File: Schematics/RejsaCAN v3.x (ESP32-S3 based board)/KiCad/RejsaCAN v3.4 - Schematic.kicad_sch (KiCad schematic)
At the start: 82 parts, among them J1 Micro-Fit 3.0 4P R/A, J2 U.FL, J3 JST-XH 4P LTE, Q1 SS8050, U1 ESP32-S3-WROOM-1(N16R8), U2 SN65HVD230DR, U3 ME2807A33M3G, U4 LMR14010ADDCR, U5 MT9700, U6 GAQY212GS, U7 LG290P03AAMD, U8 AP2112K-3.3

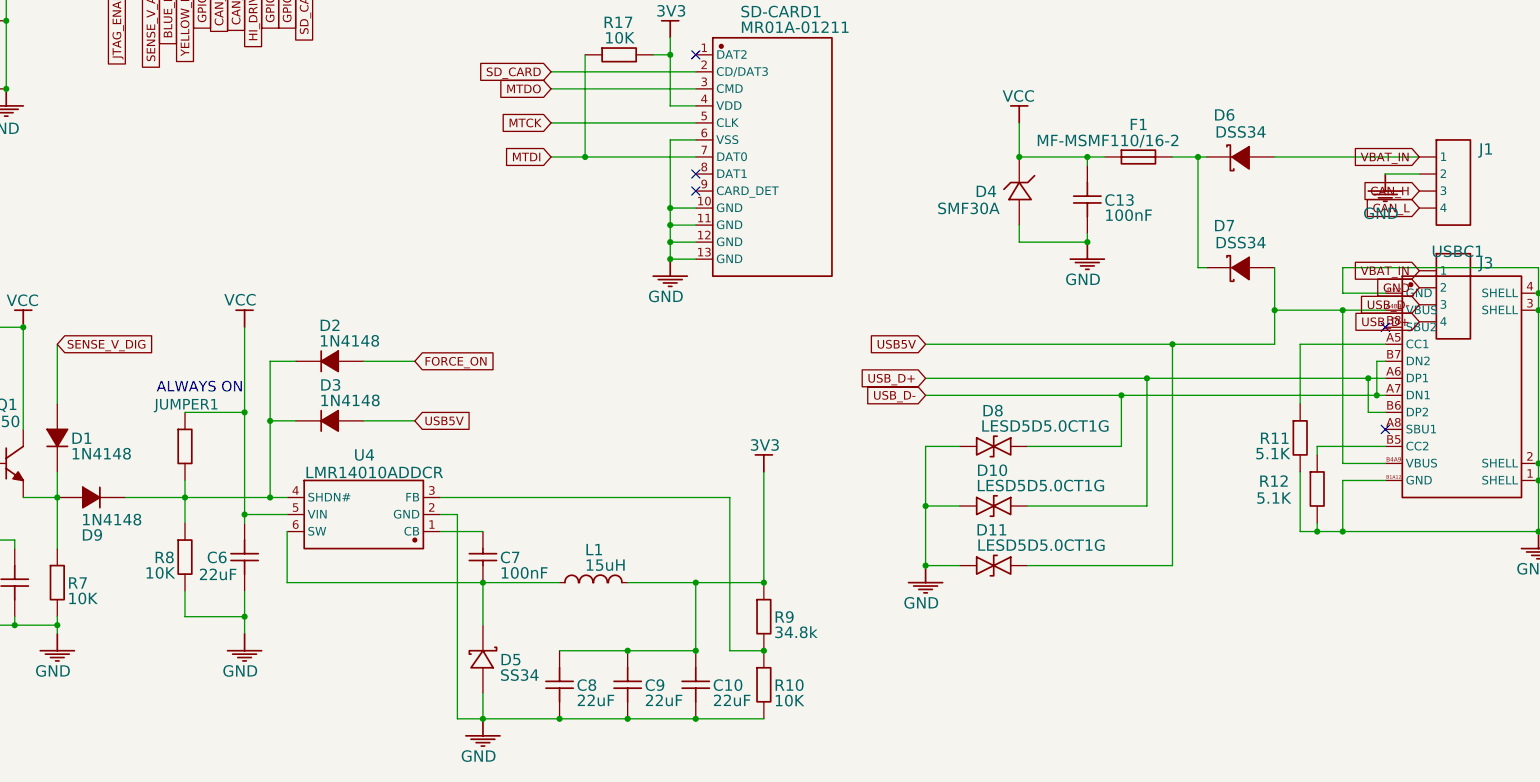
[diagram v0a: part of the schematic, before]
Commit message: Front end rated for real automotive transients: 5-24V, 33V ceiling
The board claimed 5-24V but none of its three protection devices supported it.
Owner confirmed the operating reality -- a 12V system running at 14V with
spikes -- and confirmed the installation constraint the fix depends on.

The chain that sets the rating: a 12V-system SUPPRESSED load dump is 35V for
40-400ms, so the clamp must not conduct at 35V -> 33V standoff -> VC 53.3V at
25C, ~56V hot -> the regulator must survive ~56V. That single requirement
forces every part below.

  U4   LMR14010A -> LMR51610X    45V abs max could not take any clamp that
                                 survives a 35V dump. Same SOT-23-6 land.
  R9   34.8k -> 69.8k            The new part's reference is 0.800V, not
  R10  10k   -> 22.1k            0.765V. Leaving the divider alone yields
                                 3.58V against the ESP32-S3's 3.6V absolute
                                 maximum. This would have cooked the module.
  D4   SMF30A -> SMBJ33CA        200W 10/1000us cannot address a millisecond
       and moved VCC -> VBAT_IN  event, and its clamp sat ABOVE the buck's
                                 abs max. Bidirectional, and now upstream of
                                 the fuse and blocking diode so it also covers
                                 reverse transients.
  D6   DSS34 -> SS310            40V cannot block a -53V clamp.
  D7   DSS34 -> SS310            Same node, same exposure.
  F1   MF-MSMF110/16-2 -> 2A/72V 16V max on a rail that sees a 24V jump start.
       PPTC -> time-delay fuse   It also derates to 0.60A at 85C against ~0.6A
                                 demand, so it nuisance-trips in an engine bay
                                 today. No PPTC family reaches 33V at 0.6A hot.
  F3   NEW 4A/72V                J3 fed an external LTE module from raw battery
                                 with no protection at all; the trace was the
                                 only curren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
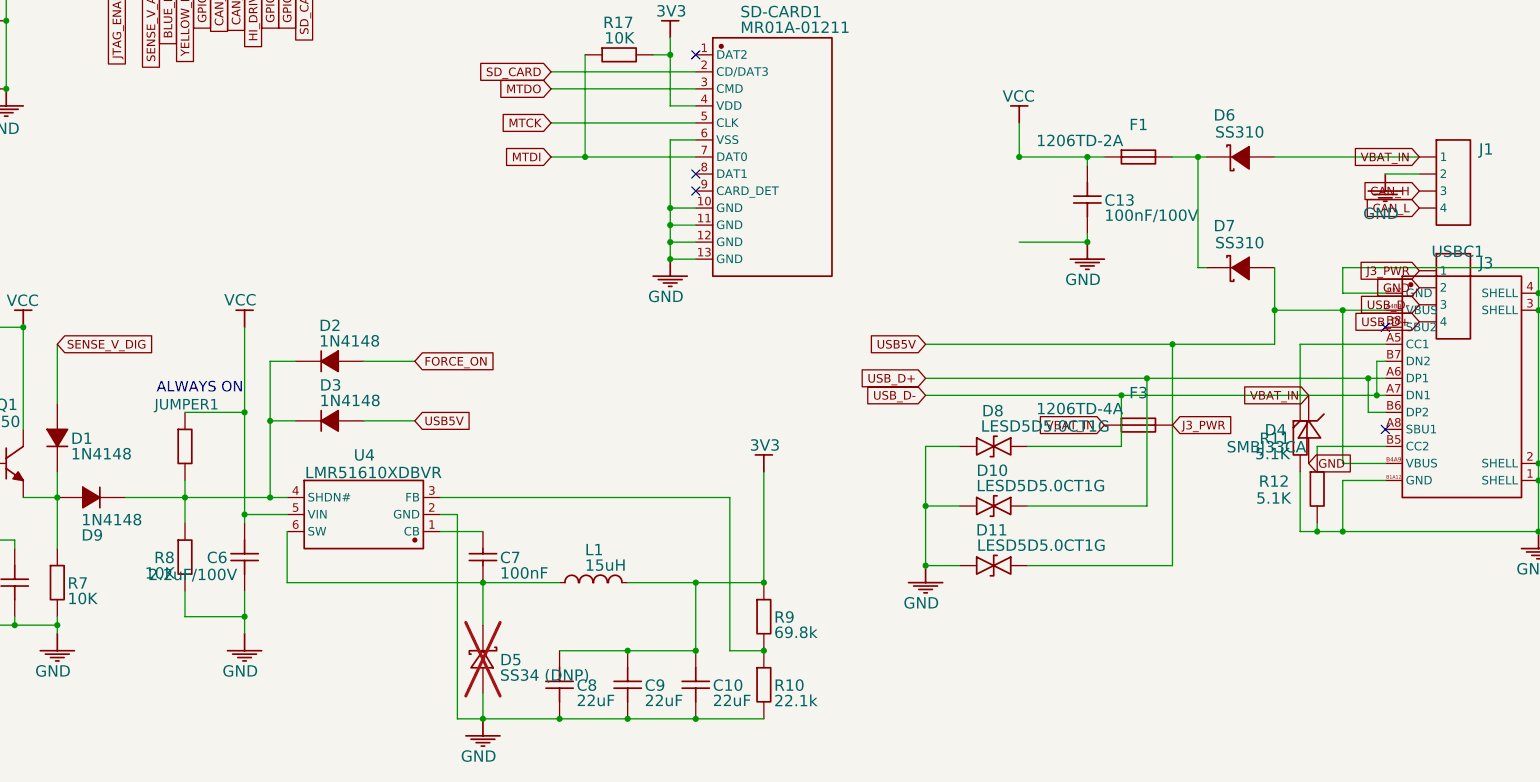
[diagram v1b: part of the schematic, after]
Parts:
- added F3: 1206TD-4A, Fuse:Fuse_1206_3216Metric, symbol MF-MSMF110/16-2
- C13: value 100nF -> 100nF/100V; footprint Capacitor_SMD:C_0402_1005Metric -> Capacitor_SMD:C_0603_1608Metric; Supplier Part C307331 -> (none)
- C6: value 22uF -> 2.2uF/100V; footprint Capacitor_SMD:C_0805_2012Metric -> Capacitor_SMD:C_1210_3225Metric; Supplier Part C602037 -> (none)
- D4: value SMF30A -> SMBJ33CA; footprint Diode_SMD:D_SOD-123 -> Diode_SMD:D_SMB; Supplier Part C366558 -> (none)
- D5: value SS34 -> SS34 (DNP); now not fitted
- D6, D7: value DSS34 -> SS310; footprint Diode_SMD:D_SOD-123 -> Diode_SMD:D_SMA; Supplier Part C84632 -> (none)
- F1: value MF-MSMF110/16-2 -> 1206TD-2A; footprint RejsaCAN:Fuse_1812_RejsaCAN_3.706mm -> Fuse:Fuse_1206_3216Metric; Supplier Part C210834 -> (none)
- R10: value 10K -> 22.1k; Supplier Part C25744 -> (none)
- R9: value 34.8k -> 69.8k; Supplier Part C25779 -> (none)
- U4: value LMR14010ADDCR -> LMR51610XDBVR
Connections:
- net USB_D-: now also D4.1, D6.2 (A), J1.1, F3.1
- net VCC: no longer D4.1
- net USB5V renamed J3_PWR
- net J3_PWR: now also J3.1, F3.2
- removed net VBAT_IN: D6.2 (A), J1.1, J3.1
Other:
- moved on the sheet: D4
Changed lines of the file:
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@@
 	(wire
 		(pts
-			(xy 200.66 121.92) (xy 200.66 119.38)
-		)
-		(stroke
-			(width 0)
-			(type default)
-		)
-	)
-	(wire
-		(pts
 			(xy 190.5 40.64) (xy 194.31 40.64)
 		)
@@
 			)
 		)
-		(property "Value" "10K"
+		(property "Value" "22.1k"
 			(at 164.084 189.3951 0)
 			(show_name no)
@@
 			)
 		)
-		(property "Supplier Part" "C25744"
+		(property "Supplier Part" ""
 			(at 162.56 187.96 0)
 			(hide yes)
@@
 			)
 		)
-		(property "Value" "22uF"
+		(property "Value" "2.2uF/100V"
 			(at 83.9978 170.5737 0)
 			(show_name no)
@@
 			)
 		)
-		(property "Footprint" "Capacitor_SMD:C_0805_2012Metric"
+		(property "Footprint" "Capacitor_SMD:C_1210_3225Metric"
 			(at 85.09 168.91 0)
 			(hide yes)
@@
 			)
 		)
-		(property "Supplier Part" "C602037"
+		(property "Supplier Part" ""
 			(at 85.09 168.91 0)
 			(hide yes)
@@
 			)
 		)
-		(property "Value" "LMR14010ADDCR"
+		(property "Value" "LMR51610XDBVR"
 			(at 94.107 155.3591 0)
 			(show_name no)
@@
 			)
 		)
-		(property "Value" "MF-MSMF110/16-2"
+		(property "Value" "1206TD-2A"
 			(at 203.2 105.8291 0)
 			(show_name no)
@@
 			)
 		)
-		(property "Footprint" "RejsaCAN:Fuse_1812_RejsaCAN_3.706mm"
+		(property "Footprint" "Fuse:Fuse_1206_3216Metric"
 			(at 218.44 109.22 0)
 			(hide yes)
@@
 			)
 		)
-		(property "Supplier Part" "C210834"
+		(property "Supplier Part" ""
 			(at 218.44 109.22 0)
 			(hide yes)
@@
 			)
 		)
-		(property "Value" "34.8k"
+		(property "Value" "69.8k"
 			(at 164.084 179.2097 0)
 			(show_name no)
@@
 			)
 		)
-		(property "Supplier Part" "C25779"
+		(property "Supplier Part" ""
 			(at 162.56 177.8 0)
 			(hide yes)
@@
 			)
 		)
-		(property "Value" "100nF"
+		(property "Value" "100nF/100V"
 			(at 213.36 116.9797 0)
 			(show_name no)
@@
 			)
 		)
-		(property "Footprint" "Capacitor_SMD:C_0402_1005Metric"
+		(property "Footprint" "Capacitor_SMD:C_0603_1608Metric"
 			(at 210.82 115.57 0)
 			(hide yes)
@@
 			)
 		)
-		(property "Supplier Part" "C307331"
+		(property "Supplier Part" ""
 			(at 210.82 115.57 0)
 			(hide yes)
@@
 			)
 		)
-		(property "Value" "DSS34"
+		(property "Value" "SS310"
 			(at 229.87 121.0691 0)
 			(show_name no)
@@
 			)
 		)
-		(property "Footprint" "Diode_SMD:D_SOD-123"
+		(property "Footprint" "Diode_SMD:D_SMA"
 			(at 233.68 125.73 0)
 			(hide yes)
@@
 			)
 		)
-		(property "Supplier Part" "C84632"
+		(property "Supplier Part" ""
 			(at 233.68 125.73 0)
 			(hide yes)
@@
 	(symbol
 		(lib_id "SMF30A_C366558")
-		(at 200.66 114.3 0)
+		(at 243.84 149.86 0)
 		(unit 0)
 		(body_style 0)
@@
 		(dnp no)
 		(property "Reference" "D4"
-			(at 194.0814 113.4237 0)
+			(at 237.261 148.984 0)
 			(show_name no)
 			(do_not_autoplace no)
@@
 			)
 		)
-		(property "Value" "SMF30A"
-			(at 188.4172 115.9637 0)
+		(property "Value" "SMBJ33CA"
+			(at 231.597 151.524 0)
 			(show_name no)
 			(do_not_autoplace no)
@@
 			)
 		)
-		(property "Footprint" "Diode_SMD:D_SOD-123"
-			(at 200.66 114.3 0)
+		(property "Footprint" "Diode_SMD:D_SMB"
+			(at 243.84 149.86 0)
 			(hide yes)
 			(show_name no)
@@
 		)
 		(property "Datasheet" ""
-			(at 200.66 114.3 0)
+			(at 243.84 149.86 0)
 			(hide yes)
 			(show_name no)
@@
 		)
 		(property "Description" ""
-			(at 200.66 114.3 0)
+			(at 243.84 149.86 0)
 			(hide yes)
 			(show_name no)
@@
 		)
 		(property "Manufacturer Part" "SMF30A"
-			(at 200.66 114.3 0)
+			(at 243.84 149.86 0)
 			(hide yes)
 			(show_name no)
@@
 		)
 		(property "Manufacturer" "DOWO"
-			(at 200.66 114.3 0)
+			(at 243.84 149.86 0)
 			(hide yes)
 			(show_name no)
@@
 			)
 		)
-		(property "Supplier Part" "C366558"
-			(at 200.66 114.3 0)
+		(property "Supplier Part" ""
+			(at 243.84 149.86 0)
 			(hide yes)
 			(show_name no)
@@
 		)
 		(property "Supplier" "LCSC"
-			(at 200.66 114.3 0)
+			(at 243.84 149.86 0)
 			(hide yes)
 			(show_name no)
@@
 		(on_board yes)
 		(in_pos_files yes)
-		(dnp no)
+		(dnp yes)
 		(property "Reference" "D5"
 			(at 123.19 183.2737 0)
@@
 			)
 		)
-		(property "Value" "SS34"
+		(property "Value" "SS34 (DNP)"
 			(at 123.19 185.5851 0)
 			(show_name no)
@@
 			)
 		)
-		(property "Value" "DSS34"
+		(property "Value" "SS310"
 			(at 229.87 104.5591 0)
 			(show_name no)
@@
 			)
 		)
-		(property "Footprint" "Diode_SMD:D_SOD-123"
+		(property "Footprint" "Diode_SMD:D_SMA"
 			(at 233.68 109.22 0)
 			(hide yes)
@@
 			)
 		)
-		(property "Supplier Part" "C84632"
+		(property "Supplier Part" ""
 			(at 233.68 109.22 0)
 			(hide yes)
@@
 		)
 	)
-	(global_label "VBAT_IN"
+	(global_label "J3_PWR"
 		(shape input)
 		(at 260.35 126.19 180)
@@
 		)
 	)
+	(global_label "VBAT_IN"
+		(shape input)
+		(at 243.84 144.78 180)
+		(effects
+			(font
+				(size 1.27 1.27)
+			)
+			(justify right)
+		)
+	)
+	(global_label "GND"
+		(shape input)
+		(at 243.84 154.94 0)
+		(effects
+			(font
+				(size 1.27 1.27)
+			)
+			(justify left)
+		)
+	)
+	(symbol
+		(lib_id "MF-MSMF110/16-2")
+		(at 218.44 149.22 0)
+		(unit 0)
+		(body_style 0)
+		(exclude_from_sim no)
+		(in_bom yes)
+		(on_board yes)
+		(in_pos_files yes)
+		(dnp no)
+		(property "Reference" "F3"
+			(at 217.068 143.441 0)
+			(show_name no)
+			(do_not_autoplace no)
+			(effects
+				(font
+					(face "Arial")
+					(size 1.6891 1.6891)
+				)
+				(justify left top)
+			)
+		)
+		(property "Value" "1206TD-4A"
+			(at 203.2 145.829 0)
+			(show_name no)
+			(do_not_autoplace no)
+			(effects
+				(font
+					(face "Arial")
+					(size 1.6891 1.6891)
+				)
+				(justify left top)
+			)
+		)
+		(property "Footprint" "Fuse:Fuse_1206_3216Metric"
+			(at 218.44 149.22 0)
+			(hide yes)
+			(show_name no)
+			(do_not_autoplace no)
+			(effects
+				(font
+					(size 1.27 1.27)
+				)
+			)
+		)
+		(property "Datasheet" ""
+			(at 218.44 149.22 0)
+			(hide yes)
+			(show_name no)
+			(do_not_autoplace no)
+			(effects
+				(font
+					(size 1.27 1.27)
+				)
+			)
+		)
+		(property "Description" ""
+			(at 218.44 149.22 0)
+			(hide yes)
+			(show_name no)
+			(do_not_autoplace no)
+			(effects
+				(font
+					(size 1.27 1.27)
+				)
+			)
+		)
+		(property "Manufacturer Part" "MF-MSMF110/16-2"
+			(at 218.44 149.22 0)
+			(hide yes)
+			(show_name no)
+			(do_not_autoplace no)
+			(effects
+				(font
+					(size 1.27 1.27)
+				)
+			)
+		)
+		(property "Manufacturer" "BOURNS"
+			(at 218.44 149.22 0)
+			(hide yes)
+			(show_name no)
+			(do_not_autoplace no)
+			(effects
+				(font
+					(size 1.27 1.27)
+				)
+			)
+		)
+		(property "Supplier Part" ""
+			(at 218.44 149.22 0)
+			(hide yes)
+			(show_name no)
+			(do_not_autoplace no)
+			(effects
+				(font
+					(size 1.27 1.27)
+				)
+			)
+		)
+		(property "Supplier" "LCSC"
+			(at 218.44 149.22 0)
+			(hide yes)
+			(show_name no)
+			(do_not_autoplace no)
+			(effects
+				(font
+					(size 1.27 1.27)
+				)
+			)
+		)
+		(pin "1"
+		)
+		(pin "2"
+		)
+		(instances
+			(project "RejsaCAN v3.4 - Schematic"
+				(path "/16c2f03a-5652-4050-b62b-75ebc6e5d249"
+					(reference "F3")
+					(unit 0)
+				)
+			)
+		)
+	)
+	(global_label "VBAT_IN"
+		(shape input)
+		(at 213.36 149.22 180)
+		(effects
+			(font
+				(size 1.27 1.27)
+			)
+			(justify right)
+		)
+	)
+	(global_label "J3_PWR"
+		(shape input)
+		(at 223.52 149.22 0)
+		(effects
+			(font
+				(size 1.27 1.27)
+			)
+			(justify left)
+		)
+	)

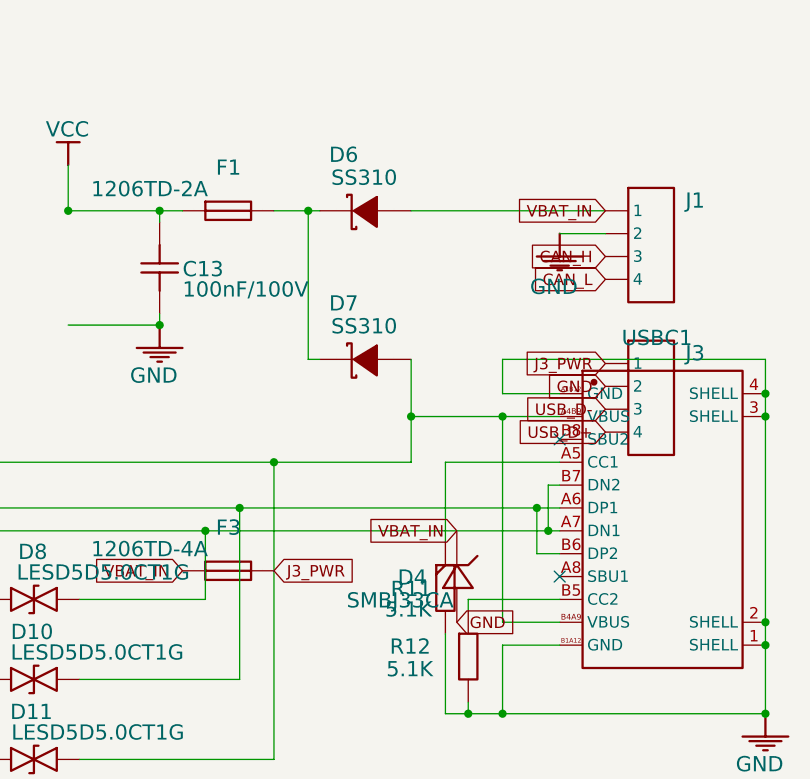
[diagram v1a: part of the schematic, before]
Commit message: PCB: rebuild for the new front end, spread the power corner, re-route
DRC clean of every electrical and fabrication class. 4 connections open, all
in the power section; finish them in the GUI's interactive router, which can
shove existing traces where the Python API cannot.

  947 tracks, 80 vias, 87 footprints
  PWR_plane  875.2 mm
  F.Cu       872.7 mm
  B.Cu       267.3 mm
  GND_plane  0 mm  -- held solid as the RF reference

Smaller packages, chosen on the numbers rather than to save space:

  D4  SMB -> SMA   SMAJ33CA. The actual pulse-1 energy is 61 mJ; SMAJ's 400 W
                   is 0.4 J, a 6.5x margin. The SMB had been sized off a figure
                   the synthesis itself flagged as ~10x high (it used 24 V
                   system pulse levels on a 12 V board).
  D6  SMA -> SOD-123FL  SS110, 100 V / 1 A. D6 carries only this board's own
  D7  SMA -> SOD-123FL  draw; the LTE branch taps VBAT_IN upstream of D6 and
                   has its own fuse, so 3 A was sizing for current that never
                   flows through it.

That took the component-area delta from +47 mm2 to +9.1 mm2 and removed the
need to grow the board.

Power corner spread. 12 low-speed parts (U3, R4, R5, R19, R6, C5, D1, D2, D9,
Q1, R7, R8 -- the battery-sense divider and the auto-shutdown chain) moved out
of the congested area. U4, L1 and D5 stayed put deliberately: they are the
switching loop, and moving them would lengthen the SW node, which already sits
45 mm from a GNSS receiver.

The split is by circuit type, not geography. The sense and shutdown circuits
are high-impedance and indifferent to a few extra millimetres; the buck is not.

Effect: the router finished in 131 s against 310-660 s on every previous
attempt, and courtyard overlaps fell 43 -> 26.

Placement was searched, not hand-picked. Three earlier attempts at choosing
coordinates by eye put C13 on the feedback divider, stacked the RF parts into
each other, and read one row of a free-space map as if the block 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
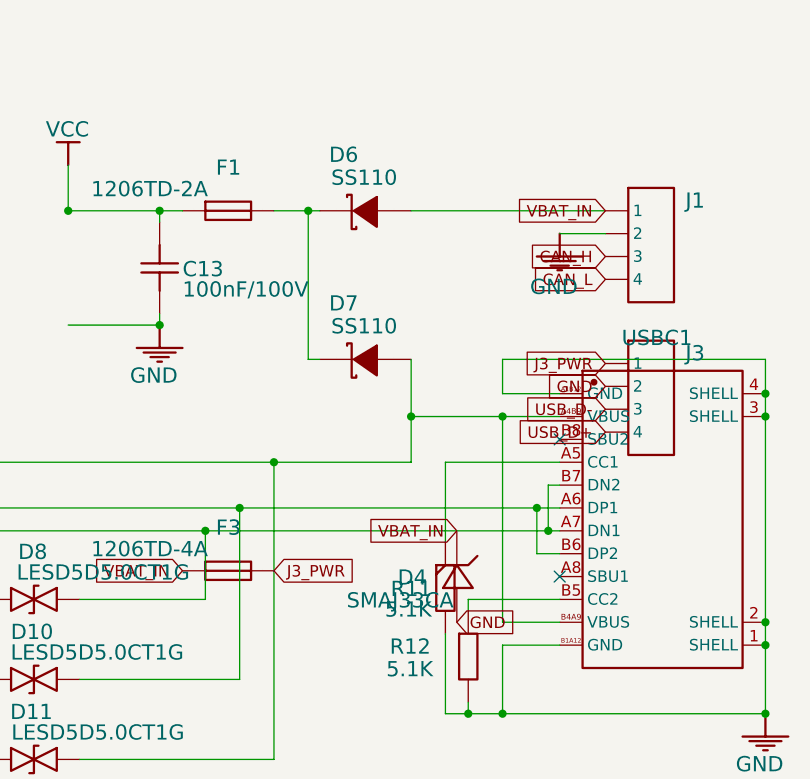
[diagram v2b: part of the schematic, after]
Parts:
- D4: value SMBJ33CA -> SMAJ33CA; footprint Diode_SMD:D_SMB -> Diode_SMD:D_SMA
- D6, D7: value SS310 -> SS110; footprint Diode_SMD:D_SMA -> Diode_SMD:D_SOD-123F
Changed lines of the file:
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@@
 			)
 		)
-		(property "Value" "SS310"
+		(property "Value" "SS110"
 			(at 229.87 121.0691 0)
 			(show_name no)
@@
 			)
 		)
-		(property "Footprint" "Diode_SMD:D_SMA"
+		(property "Footprint" "Diode_SMD:D_SOD-123F"
 			(at 233.68 125.73 0)
 			(hide yes)
@@
 			)
 		)
-		(property "Value" "SMBJ33CA"
+		(property "Value" "SMAJ33CA"
 			(at 231.597 151.524 0)
 			(show_name no)
@@
 			)
 		)
-		(property "Footprint" "Diode_SMD:D_SMB"
+		(property "Footprint" "Diode_SMD:D_SMA"
 			(at 243.84 149.86 0)
 			(hide yes)
@@
 			)
 		)
-		(property "Value" "SS310"
+		(property "Value" "SS110"
 			(at 229.87 104.5591 0)
 			(show_name no)
@@
 			)
 		)
-		(property "Footprint" "Diode_SMD:D_SMA"
+		(property "Footprint" "Diode_SMD:D_SOD-123F"
 			(at 233.68 109.22 0)
 			(hide yes)
